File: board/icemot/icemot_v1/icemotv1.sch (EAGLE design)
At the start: 2 parts, among them U1 ICE40HX4K, U2 EFM32WG332FXXX-QFP64

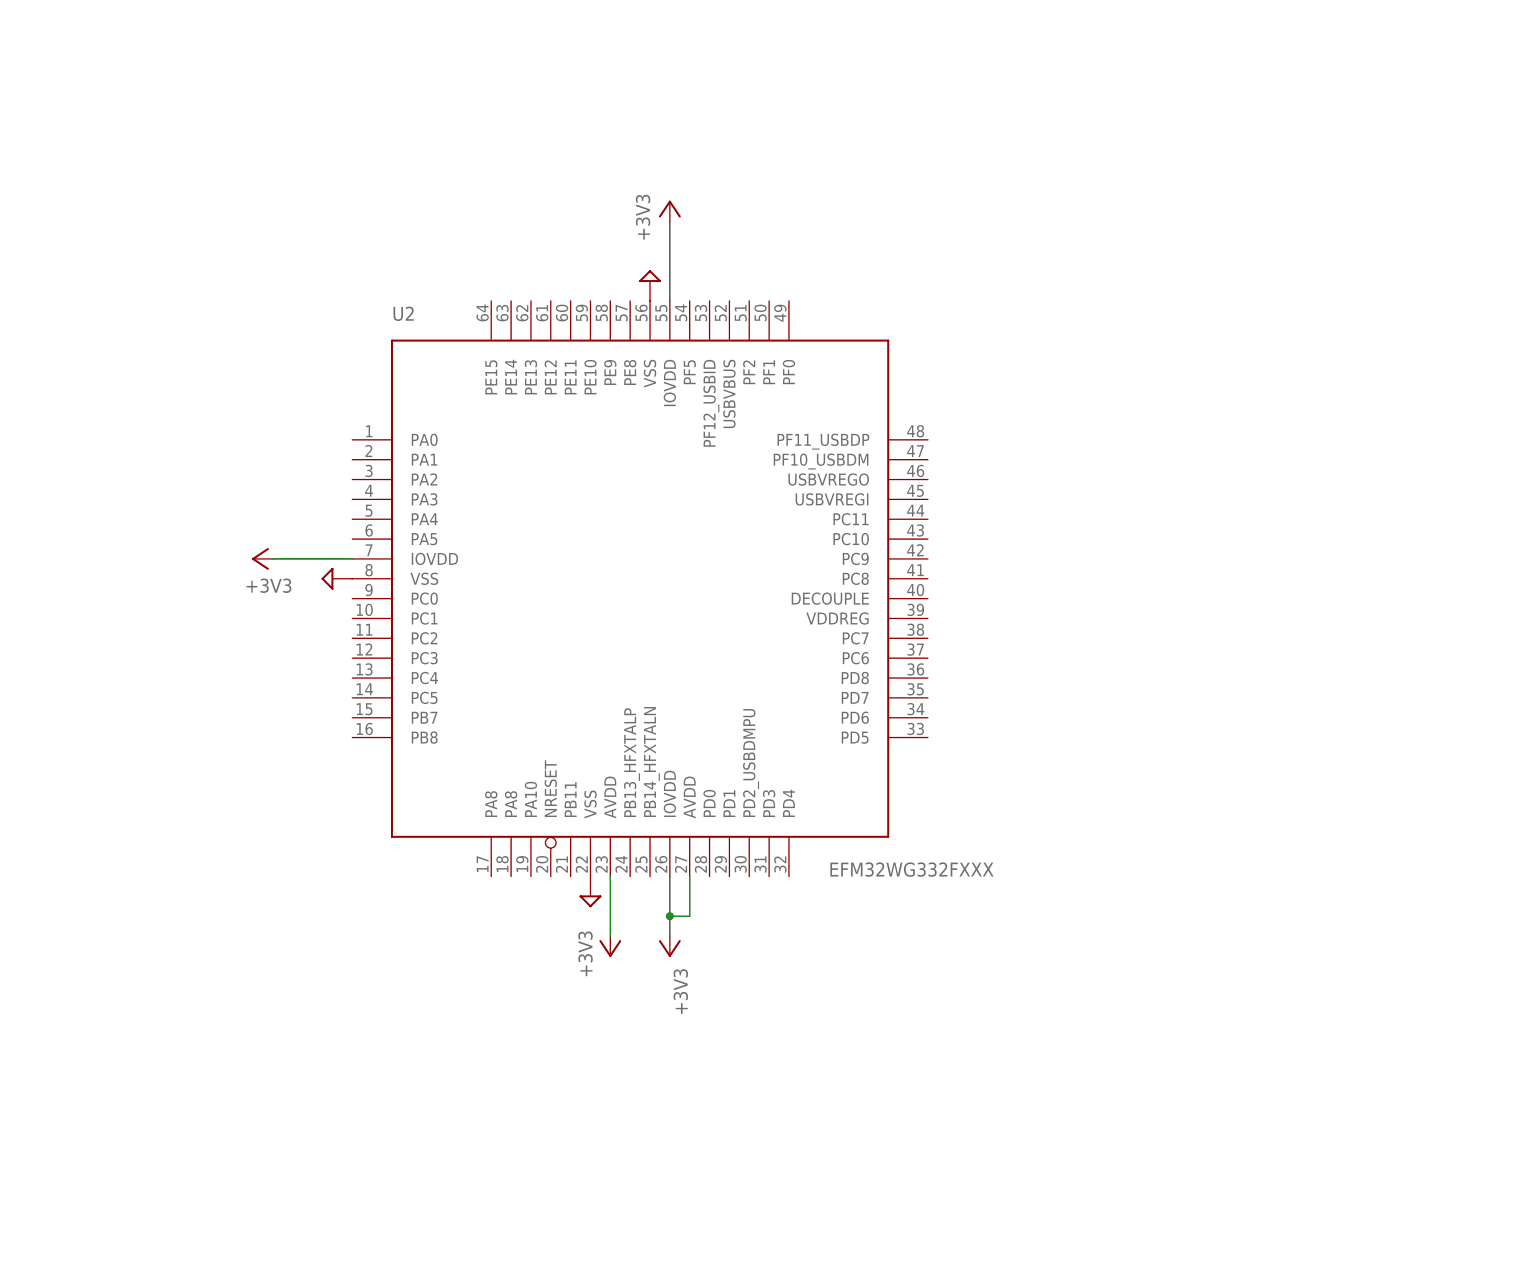
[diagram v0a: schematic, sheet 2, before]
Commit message: adding decoupling and usb connector
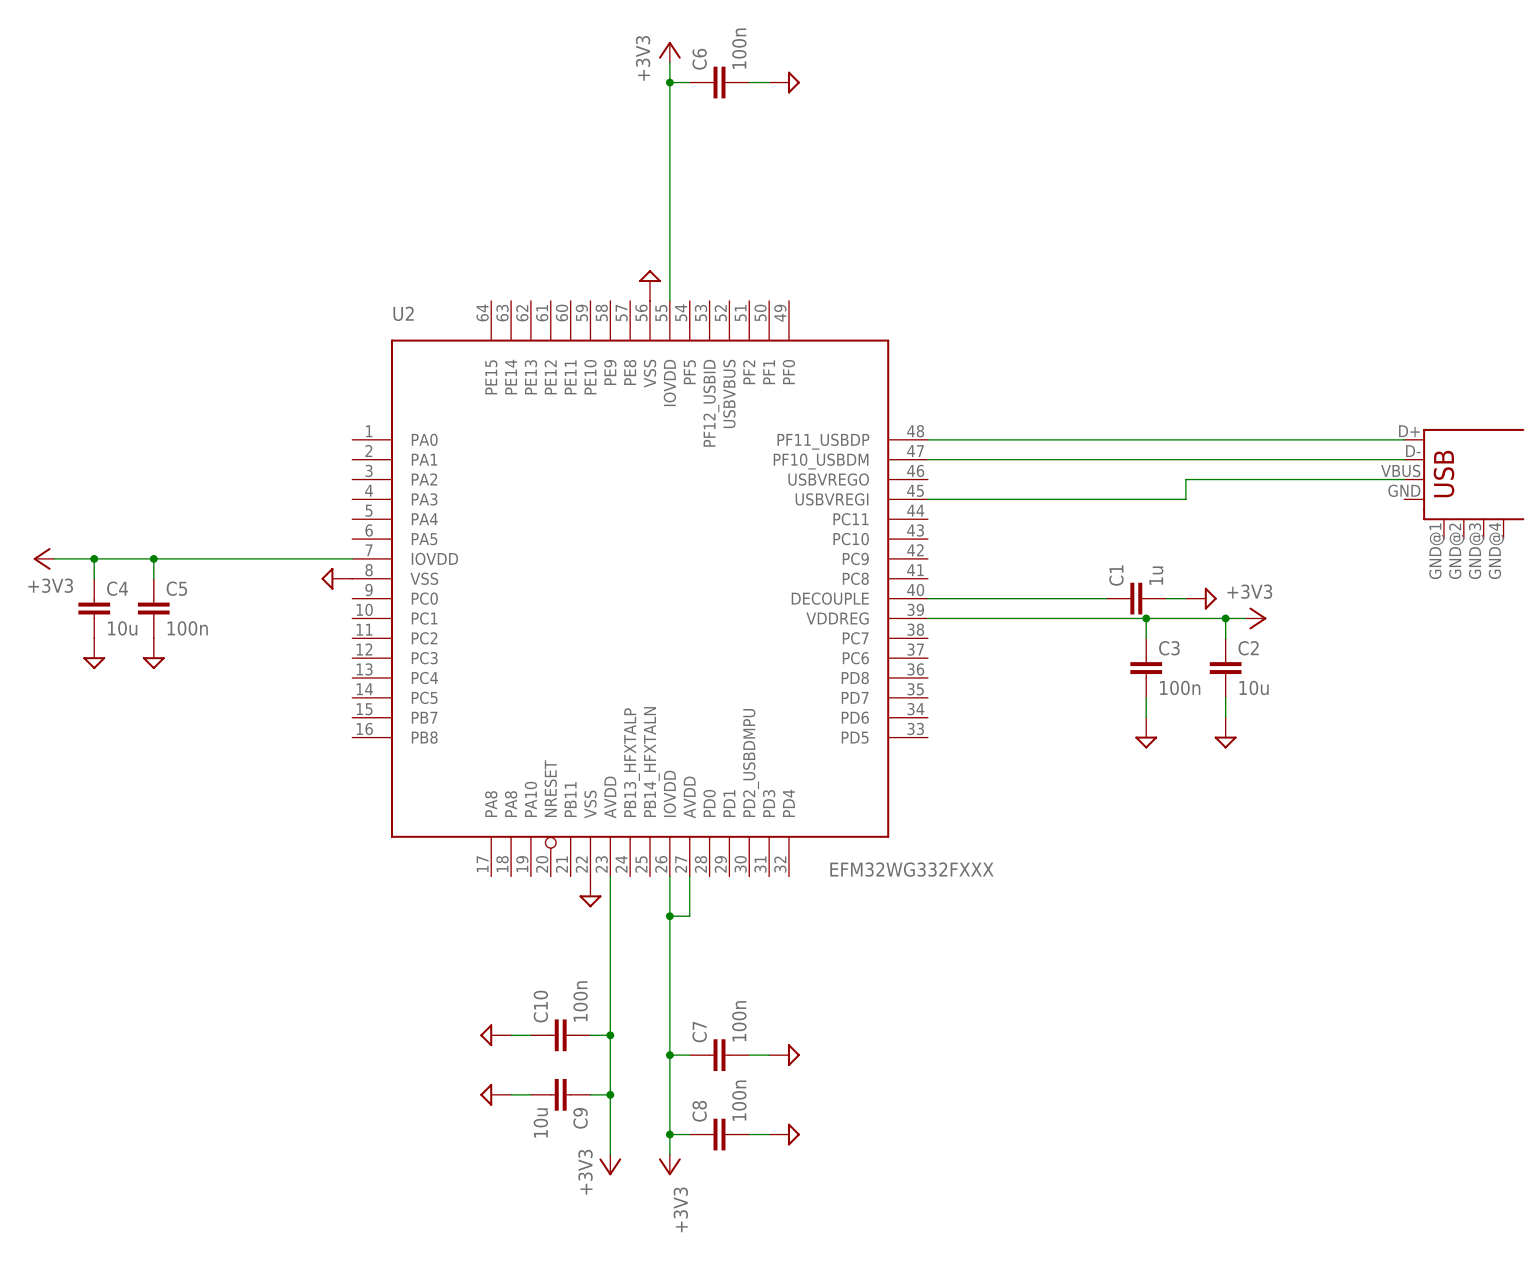
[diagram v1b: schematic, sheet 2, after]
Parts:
- added C1: 1u, standard_passive:CAP_0603
- added C10, C3, C5, C6, C7, C8: 100n, standard_passive:CAP_0603
- added C2, C4, C9: 10u, standard_passive:CAP_0805
- added U$1: USB-SHIELD, usb-header:USB-SHIELD
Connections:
- new net N$1: C1.1, U2.DECOUPLE@40
- new net N$2: U$1.D+, U2.PF11_USBDP@48
- new net N$3: U$1.D-, U2.PF10_USBDM@47
- new net N$4: U$1.VBUS, U2.USBVREGI@45
- net +3V3: now also C10.2, C2.1, C3.1, C4.1, C5.1, C6.1, C7.1, C8.1, C9.1, U2.VDDREG@39
- net GND: now also C1.2, C10.1, C2.2, C3.2, C4.2, C5.2, C6.2, C7.2, C8.2, C9.2
